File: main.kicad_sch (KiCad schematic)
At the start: 58 parts, among them J13 Conn_01x01_Female, J14 Conn_01x03_Socket

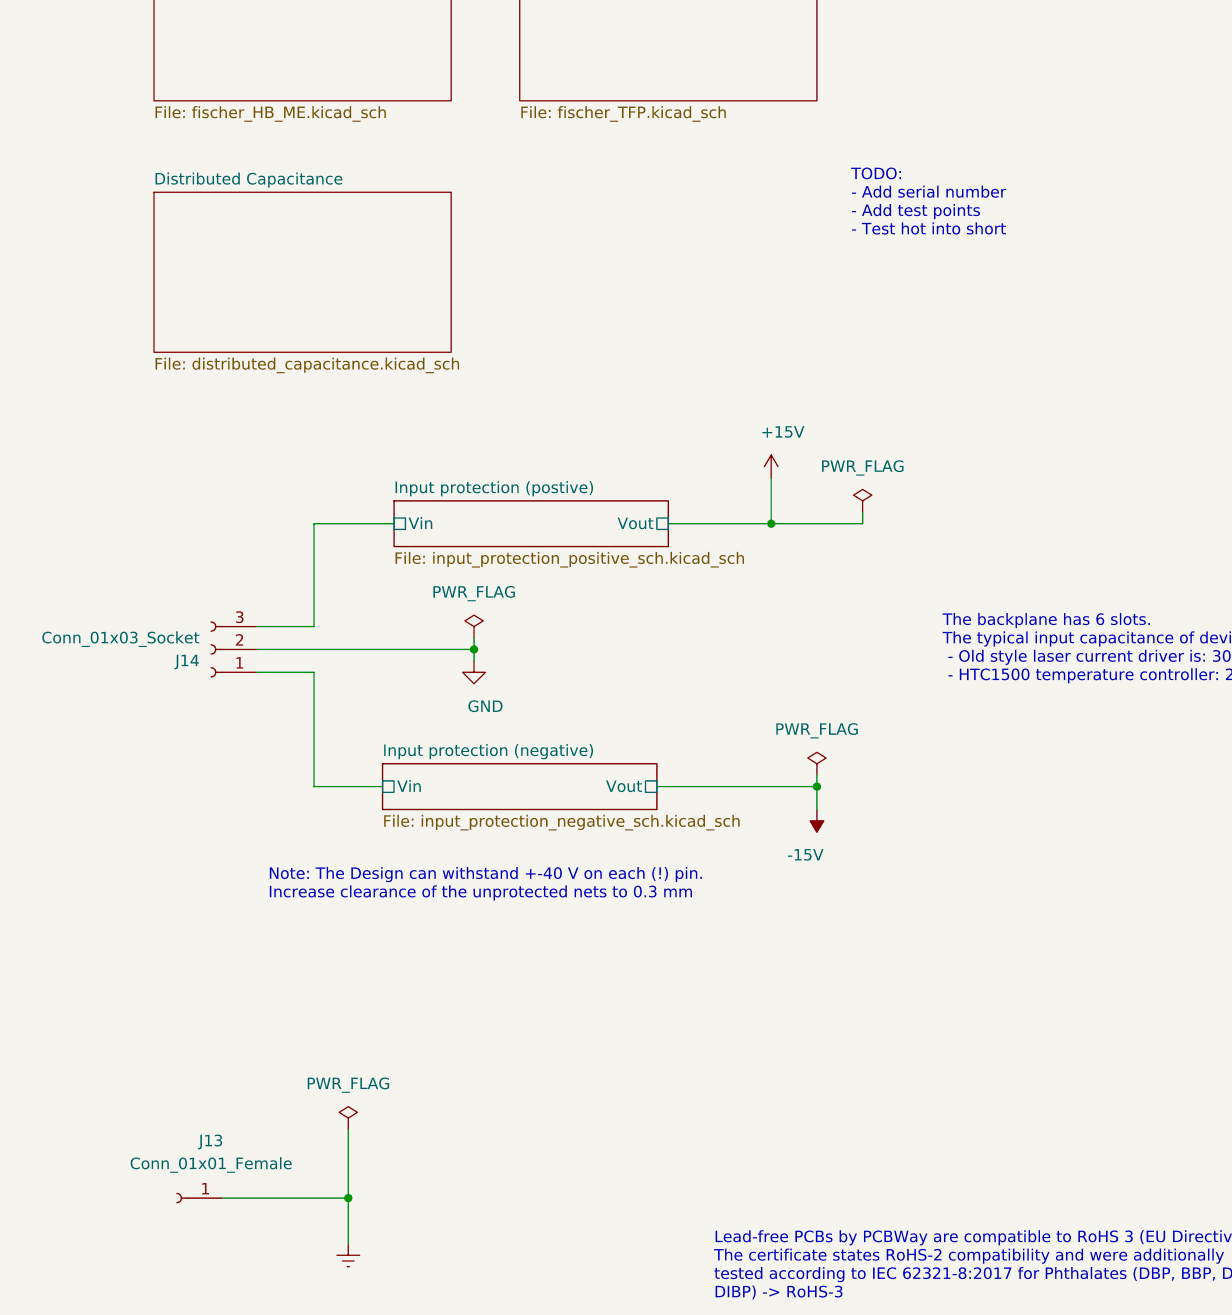
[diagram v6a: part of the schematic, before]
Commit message: Added test points
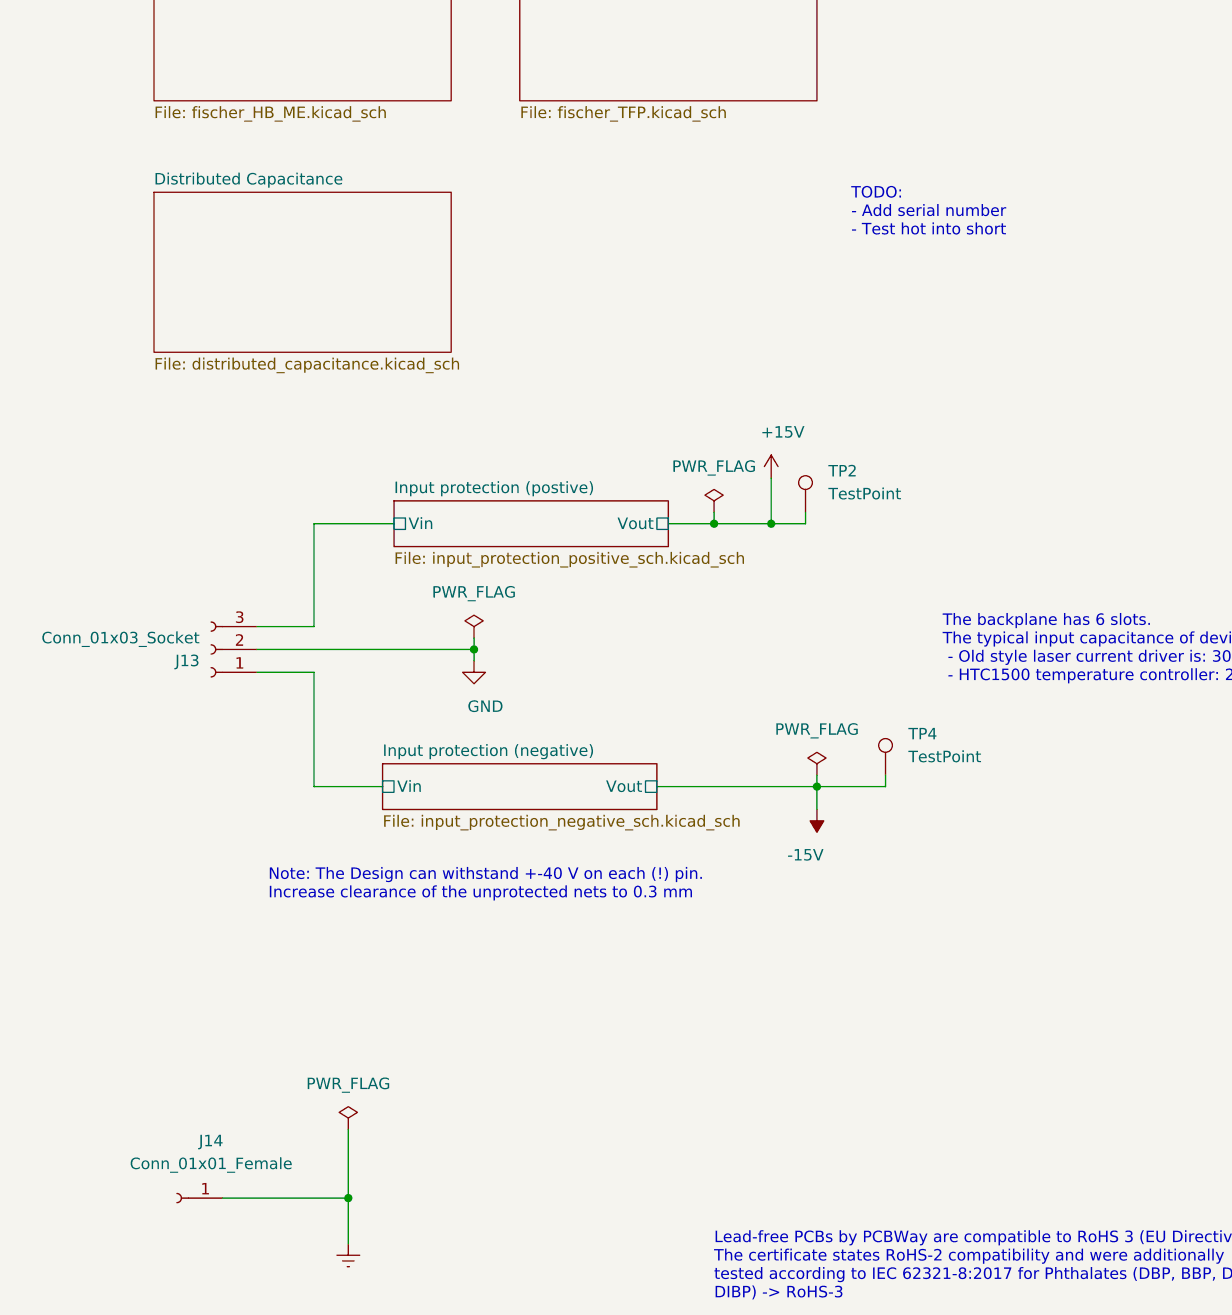
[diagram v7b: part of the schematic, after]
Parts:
- added TP2, TP4: TestPoint, TestPoint:TestPoint_Pad_D1.5mm, symbol Connector:TestPoint
- renumbered J14 to J13, J13 to J14, SYM4 to SYM1, SYM5 to SYM10, SYM3 to SYM2, SYM2 to SYM3, SYM6 to SYM4, SYM1 to SYM5, SYM8 to SYM6, SYM9 to SYM7, SYM10 to SYM8, SYM7 to SYM9
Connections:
- net +15V: now also TP2.1
- net -15V: now also TP4.1
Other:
- note added: "TODO: - Add serial number - Test hot into short"
- note removed: "TODO: - Add serial number - Add test points - Test hot into short"

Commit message: Cleaned up BOM
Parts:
- LOGO1: DNP 1 -> (none)
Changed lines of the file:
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@@
-      (effects (font (size 1.27 1.27)) hide)
-    )
-    (property "DNP" "1" (at 242.57 171.45 0)
       (effects (font (size 1.27 1.27)) hide)
     )
